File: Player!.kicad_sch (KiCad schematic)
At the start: 25 parts, among them J1 USB4085-GF-A_REVA4, SW1 SW_Push, SW2 SW_Push, SW3 SW_Push, SW4 SW_Push, SW5 RotaryEncoder_Switch

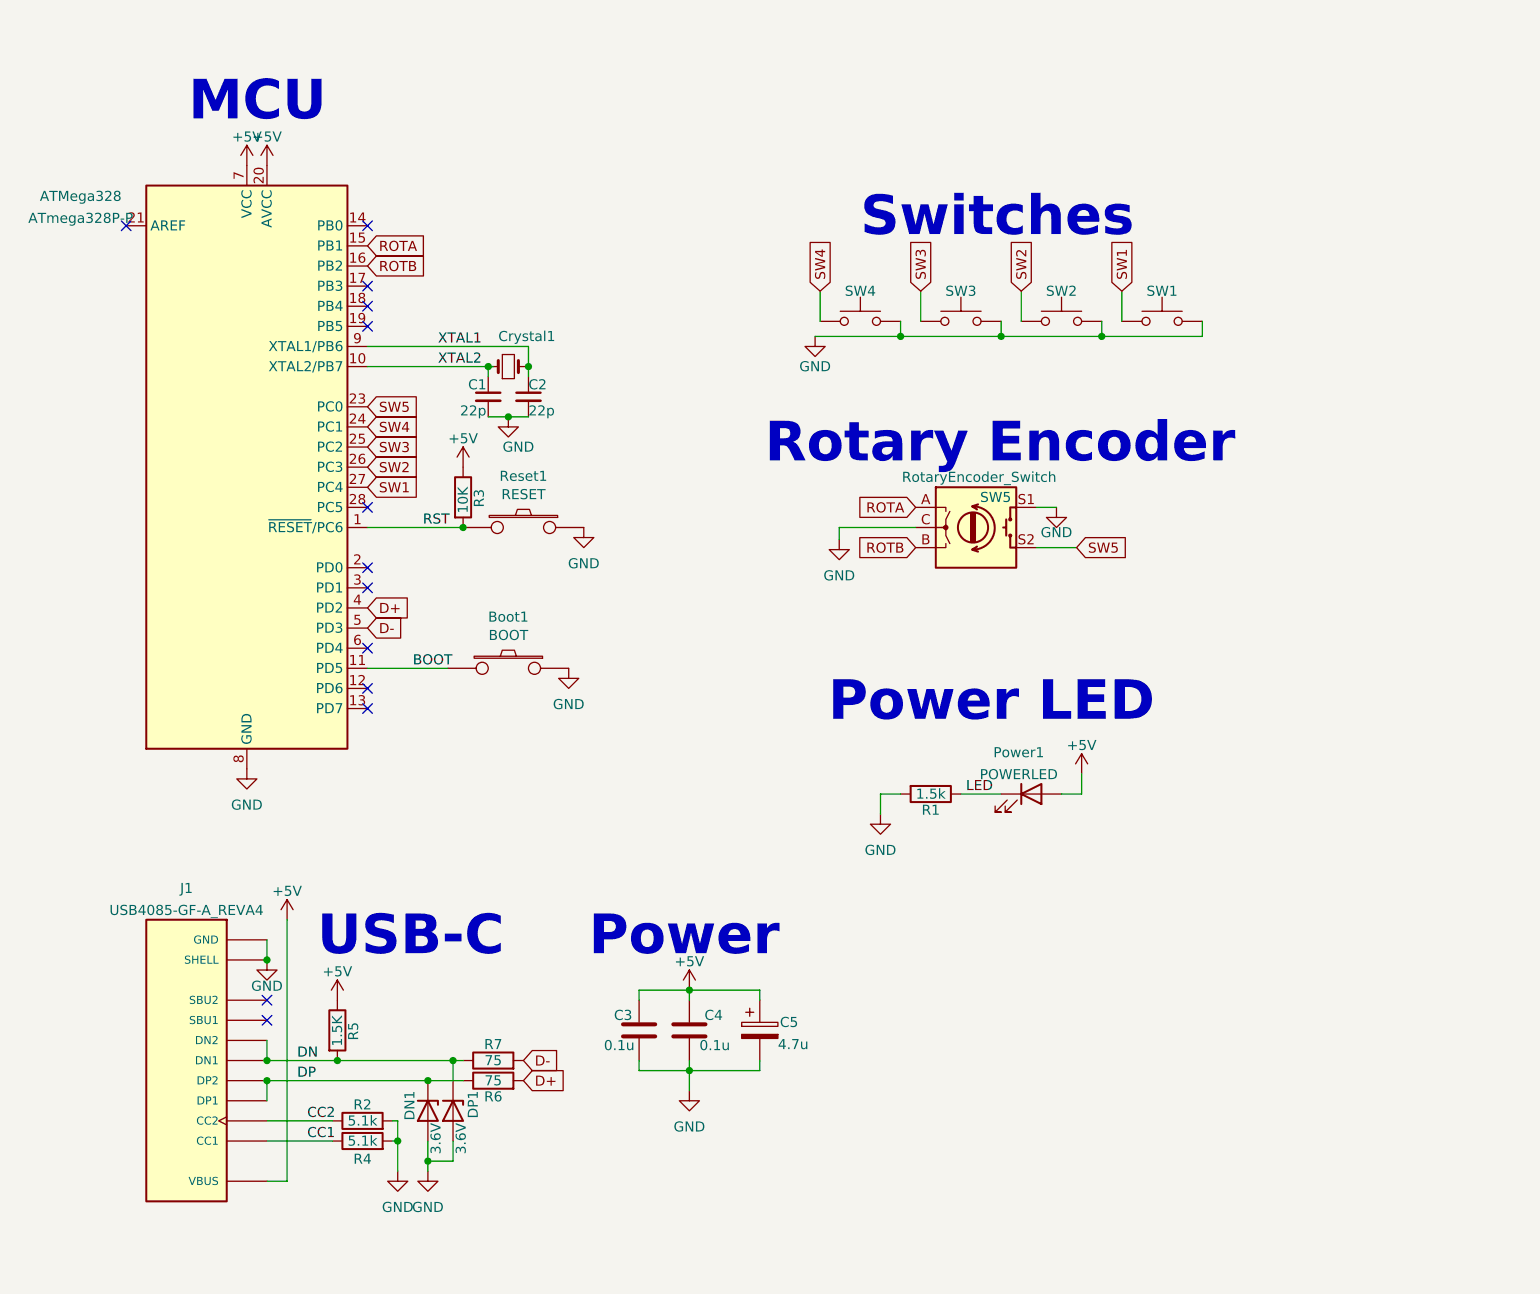
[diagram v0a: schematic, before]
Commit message: Updated to V1.31
V1.31 makes the bigger to accommodate 4 mounting holes, adds a decorative tropical pattern to the top copper plane in the otherwise blank space; numerous small changes made to improve the overall appearance. Some changes were made to footprints and their silkscreens, as well as move their reference point. Switched to Kailh hotswap sockets for the switches.
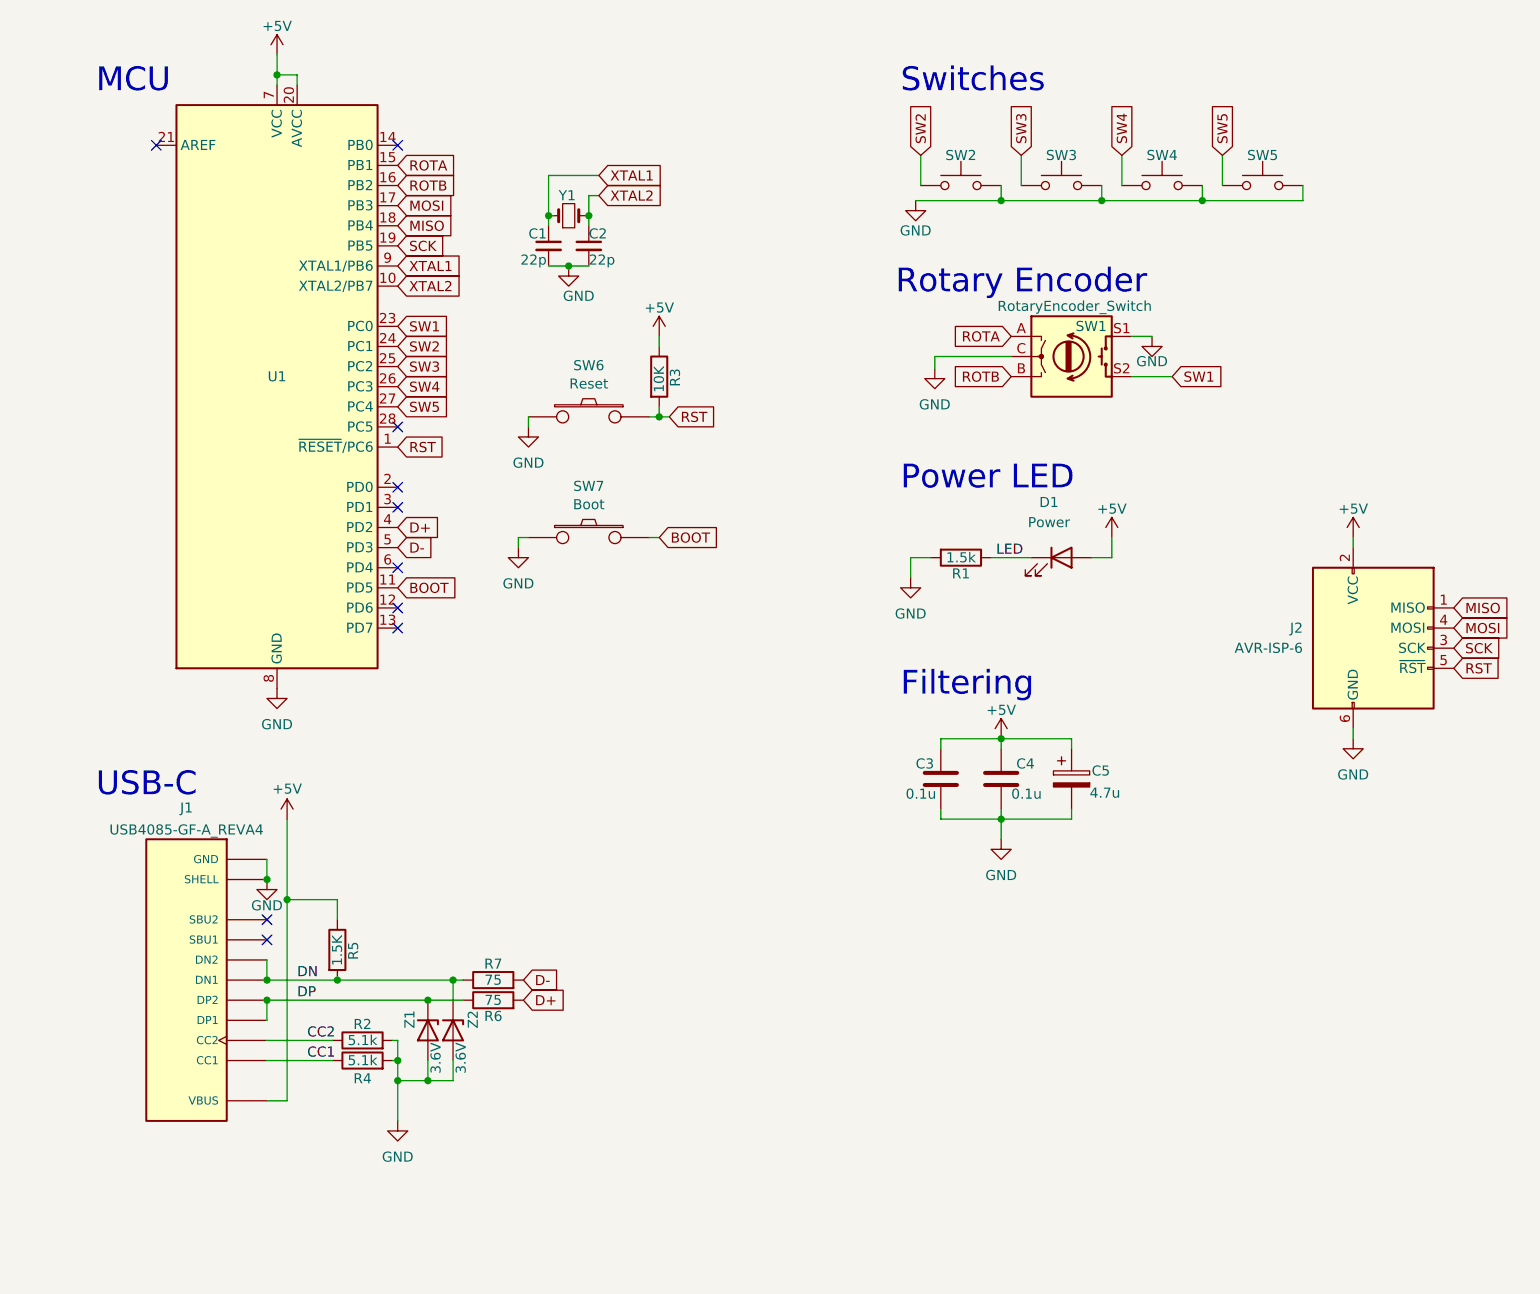
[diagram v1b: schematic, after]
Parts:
- added J2: AVR-ISP-6, Keyboard Stuff:PinHeader_2x03_P2.54mm_Vertical, symbol Connector:AVR-ISP-6
- D1: renamed from Power1; value POWERLED -> Power
- R6: footprint Keyboard_Stuff:R_Axial_DIN0204_L3.6mm_D1.6mm_P5.08mm_Horizontal -> Keyboard Stuff:R_Axial_DIN0204_L3.6mm_D1.6mm_P5.08mm_Horizontal
- R7: footprint Resistor_THT:R_Axial_DIN0204_L3.6mm_D1.6mm_P5.08mm_Horizontal -> Keyboard Stuff:R_Axial_DIN0204_L3.6mm_D1.6mm_P5.08mm_Horizontal
- SW2: renamed from SW4; footprint Keyboard Stuff:Player! 1u PCB -> Keyboard Stuff:SW_Hotswap_Kailh_MX_1.00u
- SW3: footprint Keyboard Stuff:Player! 1u PCB -> Keyboard Stuff:SW_Hotswap_Kailh_MX_1.00u
- SW4: renamed from SW2; footprint Keyboard Stuff:Player! 1u PCB -> Keyboard Stuff:SW_Hotswap_Kailh_MX_1.00u
- SW5: renamed from SW1; footprint Keyboard Stuff:Player! 1u PCB -> Keyboard Stuff:SW_Hotswap_Kailh_MX_1.00u
- SW6: renamed from Reset1; value RESET -> Reset
- SW7: renamed from Boot1; value BOOT -> Boot
- renumbered SW5 to SW1, ATMega328 to U1, Crystal1 to Y1, DN1 to Z1, DP1 to Z2
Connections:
- net +5V: now also J2.2 (VCC)
- net BOOT: now also SW7.2; no longer SW7.1
- net GND: now also SW6.1, SW7.1, J2.6 (GND); no longer SW6.2, SW7.2
- net RST: now also SW6.2, J2.5 (~{RST}); no longer SW6.1
- net SW1: now also SW1.S2, U1.23 (PC0); no longer SW5.1, U1.27 (PC4)
- net SW2: now also SW2.1, U1.24 (PC1); no longer SW4.1, U1.26 (PC3)
- net SW4: now also SW4.1, U1.26 (PC3); no longer SW2.1, U1.24 (PC1)
- net SW5: now also SW5.1, U1.27 (PC4); no longer SW1.S2, U1.23 (PC0)
- net XTAL1: now also C1.1, Y1.1; no longer C2.1, Y1.2
- net XTAL2: now also C2.1, Y1.2; no longer C1.1, Y1.1
- net MOSI: now reaches U1.17 (PB3)
- net MOSI: now also J2.4 (MOSI)
- net MISO: now reaches U1.18 (PB4)
- net MISO: now also J2.1 (MISO)
- net SCK: now reaches U1.19 (PB5)
- net SCK: now also J2.3 (SCK)
- no-connect marks 13 -> 10
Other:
- note added: "Filtering"
- note removed: "Power"
- moved on the sheet: C1, C2, C3, C4, C5, D1, J1, R1, R2, R3, R4, R5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

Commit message: Final PCB changes for v1.31
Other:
- note added: "ICSP"
- moved on the sheet: J2
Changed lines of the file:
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@@
     (stroke (width 0) (type default) (color 0 0 0 0))
   )
-  (wire (pts (xy 184.15 200.66) (xy 184.15 199.39))
+  (wire (pts (xy 144.78 262.89) (xy 144.78 261.62))
     (stroke (width 0) (type default) (color 0 0 0 0))
   )
@@
     (stroke (width 0) (type default) (color 0 0 0 0))
   )
-  (wire (pts (xy 184.15 175.26) (xy 184.15 176.53))
+  (wire (pts (xy 144.78 237.49) (xy 144.78 238.76))
     (stroke (width 0) (type default) (color 0 0 0 0))
   )
@@
   )
   (text "Filtering" (at 127 195.58 0)
+    (effects (font (size 3 3)) (justify left bottom))
+  )
+  (text "ICSP" (at 127 233.68 0)
     (effects (font (size 3 3)) (justify left bottom))
   )
@@
     )
   )
-  (global_label "SCK" (shape input) (at 196.85 189.23 0) (fields_autoplaced)
-    (effects (font (size 1.27 1.27)) (justify left))
-    (property "Intersheet References" "${INTERSHEET_REFS}" (id 0) (at 203.0126 189.1506 0)
+  (global_label "SCK" (shape input) (at 157.48 251.46 0) (fields_autoplaced)
+    (effects (font (size 1.27 1.27)) (justify left))
+    (property "Intersheet References" "${INTERSHEET_REFS}" (id 0) (at 163.6426 251.3806 0)
       (effects (font (size 1.27 1.27)) (justify left) hide)
     )
@@
     )
   )
-  (global_label "MISO" (shape input) (at 196.85 184.15 0) (fields_autoplaced)
-    (effects (font (size 1.27 1.27)) (justify left))
-    (property "Intersheet References" "${INTERSHEET_REFS}" (id 0) (at 203.8593 184.0706 0)
+  (global_label "MISO" (shape input) (at 157.48 246.38 0) (fields_autoplaced)
+    (effects (font (size 1.27 1.27)) (justify left))
+    (property "Intersheet References" "${INTERSHEET_REFS}" (id 0) (at 164.4893 246.3006 0)
       (effects (font (size 1.27 1.27)) (justify left) hide)
     )
@@
     )
   )
-  (global_label "MOSI" (shape input) (at 196.85 186.69 0) (fields_autoplaced)
-    (effects (font (size 1.27 1.27)) (justify left))
-    (property "Intersheet References" "${INTERSHEET_REFS}" (id 0) (at 203.8593 186.6106 0)
-      (effects (font (size 1.27 1.27)) (justify left) hide)
-    )
-  )
-  (global_label "RST" (shape input) (at 196.85 191.77 0) (fields_autoplaced)
-    (effects (font (size 1.27 1.27)) (justify left))
-    (property "Intersheet References" "${INTERSHEET_REFS}" (id 0) (at 202.7102 191.6906 0)
+  (global_label "MOSI" (shape input) (at 157.48 248.92 0) (fields_autoplaced)
+    (effects (font (size 1.27 1.27)) (justify left))
+    (property "Intersheet References" "${INTERSHEET_REFS}" (id 0) (at 164.4893 248.8406 0)
+      (effects (font (size 1.27 1.27)) (justify left) hide)
+    )
+  )
+  (global_label "RST" (shape input) (at 157.48 254 0) (fields_autoplaced)
+    (effects (font (size 1.27 1.27)) (justify left))
+    (property "Intersheet References" "${INTERSHEET_REFS}" (id 0) (at 163.3402 253.9206 0)
       (effects (font (size 1.27 1.27)) (justify left) hide)
     )
@@
     (pin "2")
   )
-  (symbol (lib_id "power:GND") (at 184.15 200.66 0) (unit 1)
+  (symbol (lib_id "power:GND") (at 144.78 262.89 0) (unit 1)
     (in_bom yes) (on_board yes) (fields_autoplaced)
-    (property "Reference" "#PWR0102" (id 0) (at 184.15 207.01 0)
-      (effects (font (size 1.27 1.27)) hide)
-    )
-    (property "Value" "GND" (id 1) (at 184.15 205.2225 0))
-    (property "Footprint" "" (id 2) (at 184.15 200.66 0)
-      (effects (font (size 1.27 1.27)) hide)
-    )
-    (property "Datasheet" "" (id 3) (at 184.15 200.66 0)
+    (property "Reference" "#PWR0102" (id 0) (at 144.78 269.24 0)
+      (effects (font (size 1.27 1.27)) hide)
+    )
+    (property "Value" "GND" (id 1) (at 144.78 267.4525 0))
+    (property "Footprint" "" (id 2) (at 144.78 262.89 0)
+      (effects (font (size 1.27 1.27)) hide)
+    )
+    (property "Datasheet" "" (id 3) (at 144.78 262.89 0)
       (effects (font (size 1.27 1.27)) hide)
     )
@@
     (pin "1")
   )
-  (symbol (lib_id "power:+5V") (at 184.15 175.26 0) (unit 1)
+  (symbol (lib_id "power:+5V") (at 144.78 237.49 0) (unit 1)
     (in_bom yes) (on_board yes) (fields_autoplaced)
-    (property "Reference" "#PWR0101" (id 0) (at 184.15 179.07 0)
-      (effects (font (size 1.27 1.27)) hide)
-    )
-    (property "Value" "+5V" (id 1) (at 184.15 171.6555 0))
-    (property "Footprint" "" (id 2) (at 184.15 175.26 0)
-      (effects (font (size 1.27 1.27)) hide)
-    )
-    (property "Datasheet" "" (id 3) (at 184.15 175.26 0)
+    (property "Reference" "#PWR0101" (id 0) (at 144.78 241.3 0)
+      (effects (font (size 1.27 1.27)) hide)
+    )
+    (property "Value" "+5V" (id 1) (at 144.78 233.8855 0))
+    (property "Footprint" "" (id 2) (at 144.78 237.49 0)
+      (effects (font (size 1.27 1.27)) hide)
+    )
+    (property "Datasheet" "" (id 3) (at 144.78 237.49 0)
       (effects (font (size 1.27 1.27)) hide)
     )
@@
     (pin "2")
   )
-  (symbol (lib_id "Connector:AVR-ISP-6") (at 186.69 189.23 0) (unit 1)
+  (symbol (lib_id "Connector:AVR-ISP-6") (at 147.32 251.46 0) (unit 1)
     (in_bom yes) (on_board yes) (fields_autoplaced)
-    (property "Reference" "J2" (id 0) (at 177.8 186.6899 0)
+    (property "Reference" "J2" (id 0) (at 138.43 248.9199 0)
       (effects (font (size 1.27 1.27)) (justify right))
     )
-    (property "Value" "AVR-ISP-6" (id 1) (at 177.8 189.2299 0)
+    (property "Value" "AVR-ISP-6" (id 1) (at 138.43 251.4599 0)
       (effects (font (size 1.27 1.27)) (justify right))
     )
-    (property "Footprint" "Keyboard Stuff:PinHeader_2x03_P2.54mm_Vertical" (id 2) (at 180.34 187.96 90)
-      (effects (font (size 1.27 1.27)) hide)
-    )
-    (property "Datasheet" " ~" (id 3) (at 154.305 203.2 0)
-      (effects (font (size 1.27 1.27)) hide)
-    )
+    (property "Footprint" "Keyboard Stuff:PinHeader_2x03_P2.54mm_Vertical" (id 2) (at 140.97 250.19 90)
+      (effects (font (size 1.27 1.27)) hide)
+    )
+    (property "Datasheet" " ~" (id 3) (at 114.935 265.43 0)
+      (effects (font (size 1.27 1.27)) hide)
+    )
